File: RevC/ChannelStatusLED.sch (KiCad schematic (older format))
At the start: 6 parts, among them Q1 MBT3946DW1T1, Q2 MBT3946DW1T1, U1 RAx4_4 1K, U2 RAx4_4 1K

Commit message: updates
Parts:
- Q1, Q2: RsComponentsNo (none) -> 791-6078
- R2, R3: LcscNo (none) -> C115295
- U1: LcscNo (none) -> C396839; Type (none) -> N/A
- U1, U2: LcscNo (none) -> C396839
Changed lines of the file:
@@
 $Descr A4 11693 8268
 encoding utf-8
-Sheet 10 29
+Sheet 2 29
 Title ""
 Date ""
@@
 AR Path="/5DDA78A9/5DFDF4A8" Ref="Q15"  Part="2"
 AR Path="/5DDBFE07/5DFDF4A8" Ref="Q17"  Part="2"
-F 0 "Q17" H 4575 1950 50  0000 C CNN
+F 0 "Q1" H 4575 1950 50  0000 C CNN
 F 1 "MBT3946DW1T1" H 4800 1850 50  0000 C CNN
 F 2 "Package_TO_SOT_SMD:SOT-363_SC-70-6" H 4475 2000 50  0001 C CNN
 F 3 "http://www.onsemi.com/pub_link/Collateral/MBT3946DW1T1-D.PDF" H 4275 1900 50  0001 C CNN
+F 4 " 791-6078" H 4275 1900 50  0001 C CNN "RsComponentsNo"
 	2    4275 1900
 	1    0    0    1
@@
 AR Path="/5DDA78A9/5DFDE96B" Ref="Q15"  Part="1"
 AR Path="/5DDBFE07/5DFDE96B" Ref="Q17"  Part="1"
-F 0 "Q17" H 5816 3420 50  0000 L CNN
+F 0 "Q1" H 5816 3420 50  0000 L CNN
 F 1 "MBT3946DW1T1" H 5816 3331 50  0000 L CNN
 F 2 "Package_TO_SOT_SMD:SOT-363_SC-70-6" H 5825 3475 50  0001 C CNN
 F 3 "http://www.onsemi.com/pub_link/Collateral/MBT3946DW1T1-D.PDF" H 5625 3375 50  0001 C CNN
+F 4 " 791-6078" H 5625 3375 50  0001 C CNN "RsComponentsNo"
 	1    5625 3375
 	1    0    0    -1
@@
 AR Path="/5DDA78A9/5DEB0CC3" Ref="#PWR097"  Part="1"
 AR Path="/5DDBFE07/5DEB0CC3" Ref="#PWR099"  Part="1"
-F 0 "#PWR099" H 5725 3675 50  0001 C CNN
+F 0 "#PWR013" H 5725 3675 50  0001 C CNN
 F 1 "GNDS" H 5730 3752 50  0000 C CNN
 F 2 "" H 5725 3925 50  0001 C CNN
@@
 AR Path="/5DDA78A9/5E699B7E" Ref="#PWR035"  Part="1"
 AR Path="/5DDBFE07/5E699B7E" Ref="#PWR037"  Part="1"
-F 0 "#PWR037" H 4375 2400 50  0001 C CNN
+F 0 "#PWR07" H 4375 2400 50  0001 C CNN
 F 1 "GNDS" H 4380 2477 50  0000 C CNN
 F 2 "" H 4375 2650 50  0001 C CNN
@@
 AR Path="/5DDA78A9/5E815CA3" Ref="Q16"  Part="1"
 AR Path="/5DDBFE07/5E815CA3" Ref="Q18"  Part="1"
-F 0 "Q18" H 3740 6196 50  0000 L CNN
+F 0 "Q2" H 3740 6196 50  0000 L CNN
 F 1 "MBT3946DW1T1" H 3740 6105 50  0000 L CNN
 F 2 "Package_TO_SOT_SMD:SOT-363_SC-70-6" H 3750 6250 50  0001 C CNN
 F 3 "http://www.onsemi.com/pub_link/Collateral/MBT3946DW1T1-D.PDF" H 3550 6150 50  0001 C CNN
+F 4 " 791-6078" H 3550 6150 50  0001 C CNN "RsComponentsNo"
 	1    3550 6150
 	1    0    0    -1
@@
 AR Path="/5DDA78A9/5E81663D" Ref="Q16"  Part="2"
 AR Path="/5DDBFE07/5E81663D" Ref="Q18"  Part="2"
-F 0 "Q18" V 7800 5100 50  0000 C CNN
+F 0 "Q2" V 7800 5100 50  0000 C CNN
 F 1 "MBT3946DW1T1" V 7700 5325 50  0000 C CNN
 F 2 "Package_TO_SOT_SMD:SOT-363_SC-70-6" H 8100 4925 50  0001 C CNN
 F 3 "http://www.onsemi.com/pub_link/Collateral/MBT3946DW1T1-D.PDF" H 7900 4825 50  0001 C CNN
+F 4 " 791-6078" V 7900 4825 50  0001 C CNN "RsComponentsNo"
 	2    7900 4825
 	0    1    -1   0
@@
 AR Path="/5DDA78A9/5E819F8C" Ref="#PWR034"  Part="1"
 AR Path="/5DDBFE07/5E819F8C" Ref="#PWR036"  Part="1"
-F 0 "#PWR036" H 3650 7150 50  0001 C CNN
+F 0 "#PWR02" H 3650 7150 50  0001 C CNN
 F 1 "GNDS" H 3655 7227 50  0000 C CNN
 F 2 "" H 3650 7400 50  0001 C CNN
@@
 AR Path="/5DDA78A9/5E833FE4" Ref="R22"  Part="1"
 AR Path="/5DDBFE07/5E833FE4" Ref="R24"  Part="1"
-F 0 "R24" H 9600 4075 50  0000 C CNN
+F 0 "R3" H 9600 4075 50  0000 C CNN
 F 1 "10K" H 9600 4175 50  0000 C CNN
 F 2 "Resistor_SMD:R_0805_2012Metric_Pad1.15x1.40mm_HandSolder" V 9705 4125 50  0001 C CNN
 F 3 "~" H 9775 4125 50  0001 C CNN
+F 4 "C115295" H 9775 4125 50  0001 C CNN "LcscNo"
 	1    9775 4125
 	-1   0    0    1
@@
 AR Path="/5DDA78A9/5E846344" Ref="R21"  Part="1"
 AR Path="/5DDBFE07/5E846344" Ref="R23"  Part="1"
-F 0 "R23" V 2146 6450 50  0000 C CNN
+F 0 "R2" V 2146 6450 50  0000 C CNN
 F 1 "10K" V 2235 6450 50  0000 C CNN
 F 2 "Resistor_SMD:R_0805_2012Metric_Pad1.15x1.40mm_HandSolder" V 2280 6450 50  0001 C CNN
 F 3 "~" H 2350 6450 50  0001 C CNN
+F 4 "C115295" V 2350 6450 50  0001 C CNN "LcscNo"
 	1    2350 6450
 	-1   0    0    1
@@
 AR Path="/5DDA78A9/5E9652F8" Ref="U15"  Part="1"
 AR Path="/5DDBFE07/5E9652F8" Ref="U17"  Part="1"
-F 0 "U17" H 3600 2125 50  0000 C CNN
+F 0 "U1" H 3600 2125 50  0000 C CNN
 F 1 "RAx4_4 1K" H 3600 2034 50  0000 C CNN
 F 2 "Resistor_SMD:R_Array_Convex_4x0603" H 3600 1800 50  0001 C CNN
-F 3 "" H 3600 1900 50  0001 C CNN
+F 3 "https://datasheet.lcsc.com/szlcsc/1912111437_HX-hengjiaxing-HX2301A_C296298.pdf" H 3600 1900 50  0001 C CNN
+F 4 "N/A" H 3600 1900 50  0001 C CNN "Type"
+F 5 "C396839" H 3600 1900 50  0001 C CNN "LcscNo"
 	1    3600 1900
 	1    0    0    -1
@@
 AR Path="/5DDA78A9/5E9687B5" Ref="U15"  Part="2"
 AR Path="/5DDBFE07/5E9687B5" Ref="U17"  Part="2"
-F 0 "U17" H 7175 2218 50  0000 C CNN
+F 0 "U1" H 7175 2218 50  0000 C CNN
 F 1 "RAx4_4 1K" H 7175 2309 50  0000 C CNN
 F 2 "Resistor_SMD:R_Array_Convex_4x0603" H 7175 2325 50  0001 C CNN
-F 3 "" H 7175 2425 50  0001 C CNN
+F 3 "https://datasheet.lcsc.com/szlcsc/1912111437_HX-hengjiaxing-HX2301A_C296298.pdf" H 7175 2425 50  0001 C CNN
+F 4 "C396839" H 7175 2425 50  0001 C CNN "LcscNo"
 	2    7175 2425
 	-1   0    0    1
@@
 AR Path="/5DDA78A9/5E96B96B" Ref="U15"  Part="3"
 AR Path="/5DDBFE07/5E96B96B" Ref="U17"  Part="3"
-F 0 "U17" V 4421 2330 50  0000 R CNN
+F 0 "U1" V 4421 2330 50  0000 R CNN
 F 1 "RAx4_4 1K" V 4330 2330 50  0000 R CNN
 F 2 "Resistor_SMD:R_Array_Convex_4x0603" H 4375 2300 50  0001 C CNN
-F 3 "" H 4375 2400 50  0001 C CNN
+F 3 "https://datasheet.lcsc.com/szlcsc/1912111437_HX-hengjiaxing-HX2301A_C296298.pdf" H 4375 2400 50  0001 C CNN
+F 4 "C396839" V 4375 2400 50  0001 C CNN "LcscNo"
 	3    4375 2400
 	0    -1   -1   0
@@
 AR Path="/5DDA78A9/5E96FE7B" Ref="U15"  Part="4"
 AR Path="/5DDBFE07/5E96FE7B" Ref="U17"  Part="4"
-F 0 "U17" H 3625 3600 50  0000 C CNN
+F 0 "U1" H 3625 3600 50  0000 C CNN
 F 1 "RAx4_4 1K" H 3625 3509 50  0000 C CNN
 F 2 "Resistor_SMD:R_Array_Convex_4x0603" H 3625 3275 50  0001 C CNN
-F 3 "" H 3625 3375 50  0001 C CNN
+F 3 "https://datasheet.lcsc.com/szlcsc/1912111437_HX-hengjiaxing-HX2301A_C296298.pdf" H 3625 3375 50  0001 C CNN
+F 4 "C396839" H 3625 3375 50  0001 C CNN "LcscNo"
 	4    3625 3375
 	1    0    0    -1
@@
 AR Path="/5DDA78A9/5E9776FE" Ref="U16"  Part="2"
 AR Path="/5DDBFE07/5E9776FE" Ref="U18"  Part="2"
-F 0 "U18" V 6854 4463 50  0000 L CNN
+F 0 "U2" V 6854 4463 50  0000 L CNN
 F 1 "RAx4_4 1K" V 6945 4463 50  0000 L CNN
 F 2 "Resistor_SMD:R_Array_Convex_4x0603" H 6900 4275 50  0001 C CNN
-F 3 "" H 6900 4375 50  0001 C CNN
+F 3 "https://datasheet.lcsc.com/szlcsc/1912111437_HX-hengjiaxing-HX2301A_C296298.pdf" H 6900 4375 50  0001 C CNN
+F 4 "C396839" V 6900 4375 50  0001 C CNN "LcscNo"
 	2    6900 4375
 	0    1    1    0
@@
 AR Path="/5DDA78A9/5E99998D" Ref="U16"  Part="3"
 AR Path="/5DDBFE07/5E99998D" Ref="U18"  Part="3"
-F 0 "U18" H 2950 6375 50  0000 C CNN
+F 0 "U2" H 2950 6375 50  0000 C CNN
 F 1 "RAx4_4 1K" H 2950 6284 50  0000 C CNN
 F 2 "Resistor_SMD:R_Array_Convex_4x0603" H 2950 6050 50  0001 C CNN
-F 3 "" H 2950 6150 50  0001 C CNN
+F 3 "https://datasheet.lcsc.com/szlcsc/1912111437_HX-hengjiaxing-HX2301A_C296298.pdf" H 2950 6150 50  0001 C CNN
+F 4 "C396839" H 2950 6150 50  0001 C CNN "LcscNo"
 	3    2950 6150
 	1    0    0    -1
@@
 AR Path="/5DDA78A9/5EAAD0E5" Ref="U16"  Part="4"
 AR Path="/5DDBFE07/5EAAD0E5" Ref="U18"  Part="4"
-F 0 "U18" V 3696 6880 50  0000 R CNN
+F 0 "U2" V 3696 6880 50  0000 R CNN
 F 1 "RAx4_4 1K" V 3605 6880 50  0000 R CNN
 F 2 "Resistor_SMD:R_Array_Convex_4x0603" H 3650 6850 50  0001 C CNN
-F 3 "" H 3650 6950 50  0001 C CNN
+F 3 "https://datasheet.lcsc.com/szlcsc/1912111437_HX-hengjiaxing-HX2301A_C296298.pdf" H 3650 6950 50  0001 C CNN
+F 4 "C396839" V 3650 6950 50  0001 C CNN "LcscNo"
 	4    3650 6950
 	0    -1   -1   0
@@
 AR Path="/5DDA78A9/5E033493" Ref="#PWR0149"  Part="1"
 AR Path="/5DDBFE07/5E033493" Ref="#PWR0150"  Part="1"
-F 0 "#PWR0150" H 2350 6900 50  0001 C CNN
+F 0 "#PWR0115" H 2350 6900 50  0001 C CNN
 F 1 "GNDS" H 2355 6977 50  0000 C CNN
 F 2 "" H 2350 7150 50  0001 C CNN

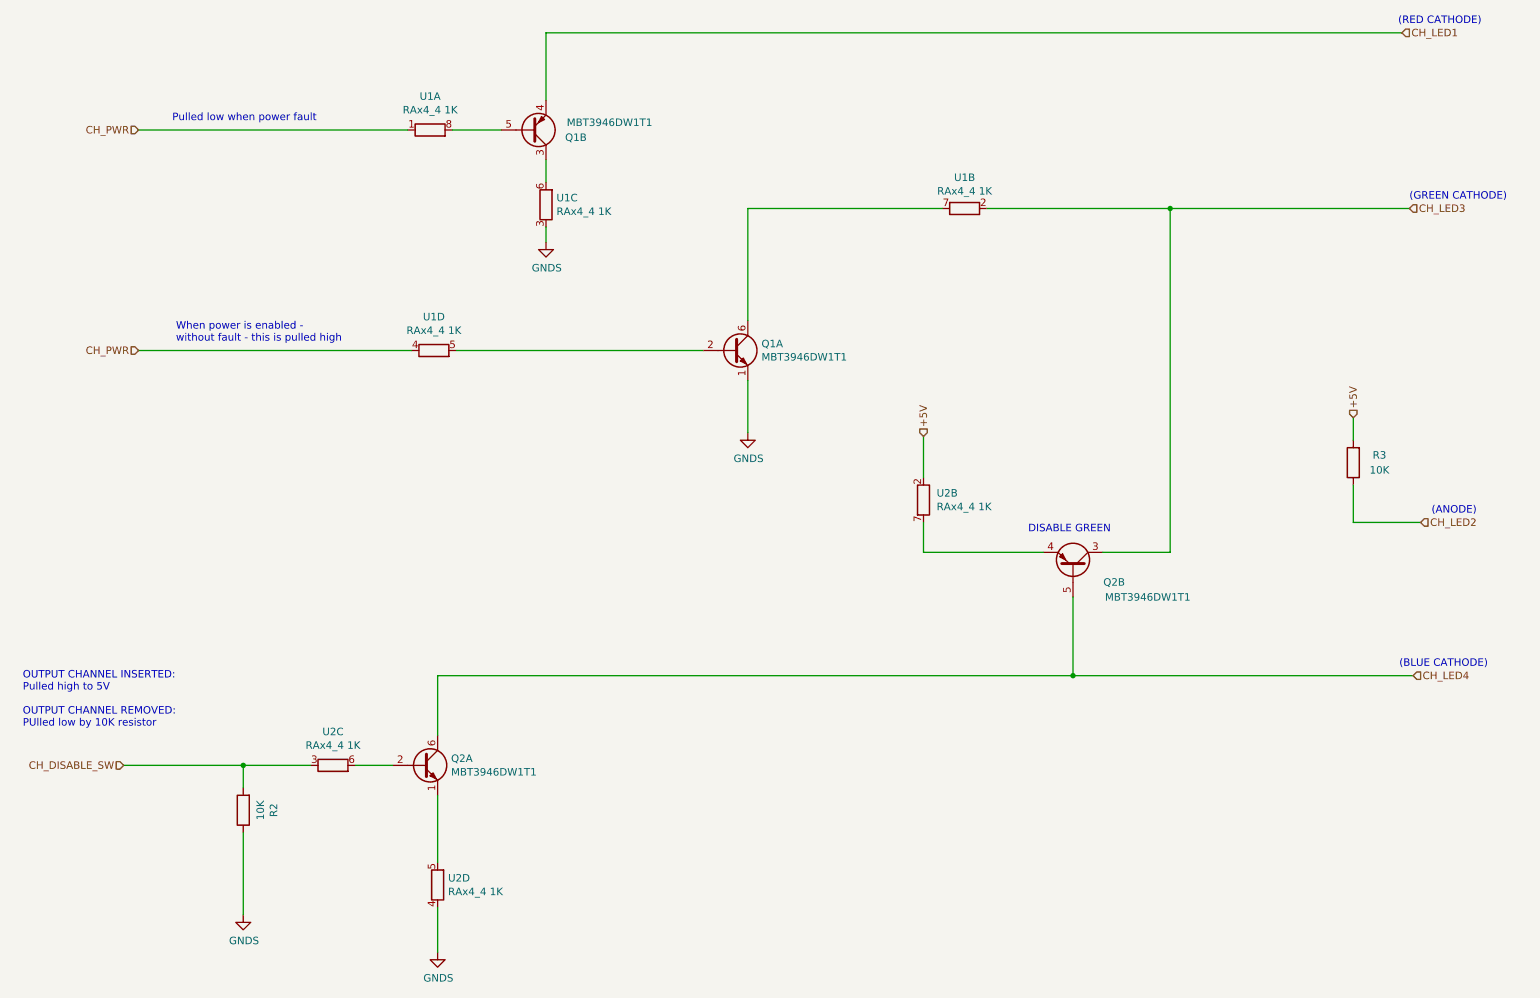
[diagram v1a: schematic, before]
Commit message: Replaced 6N135 SMDIP8 with H11L1 SMDIP6
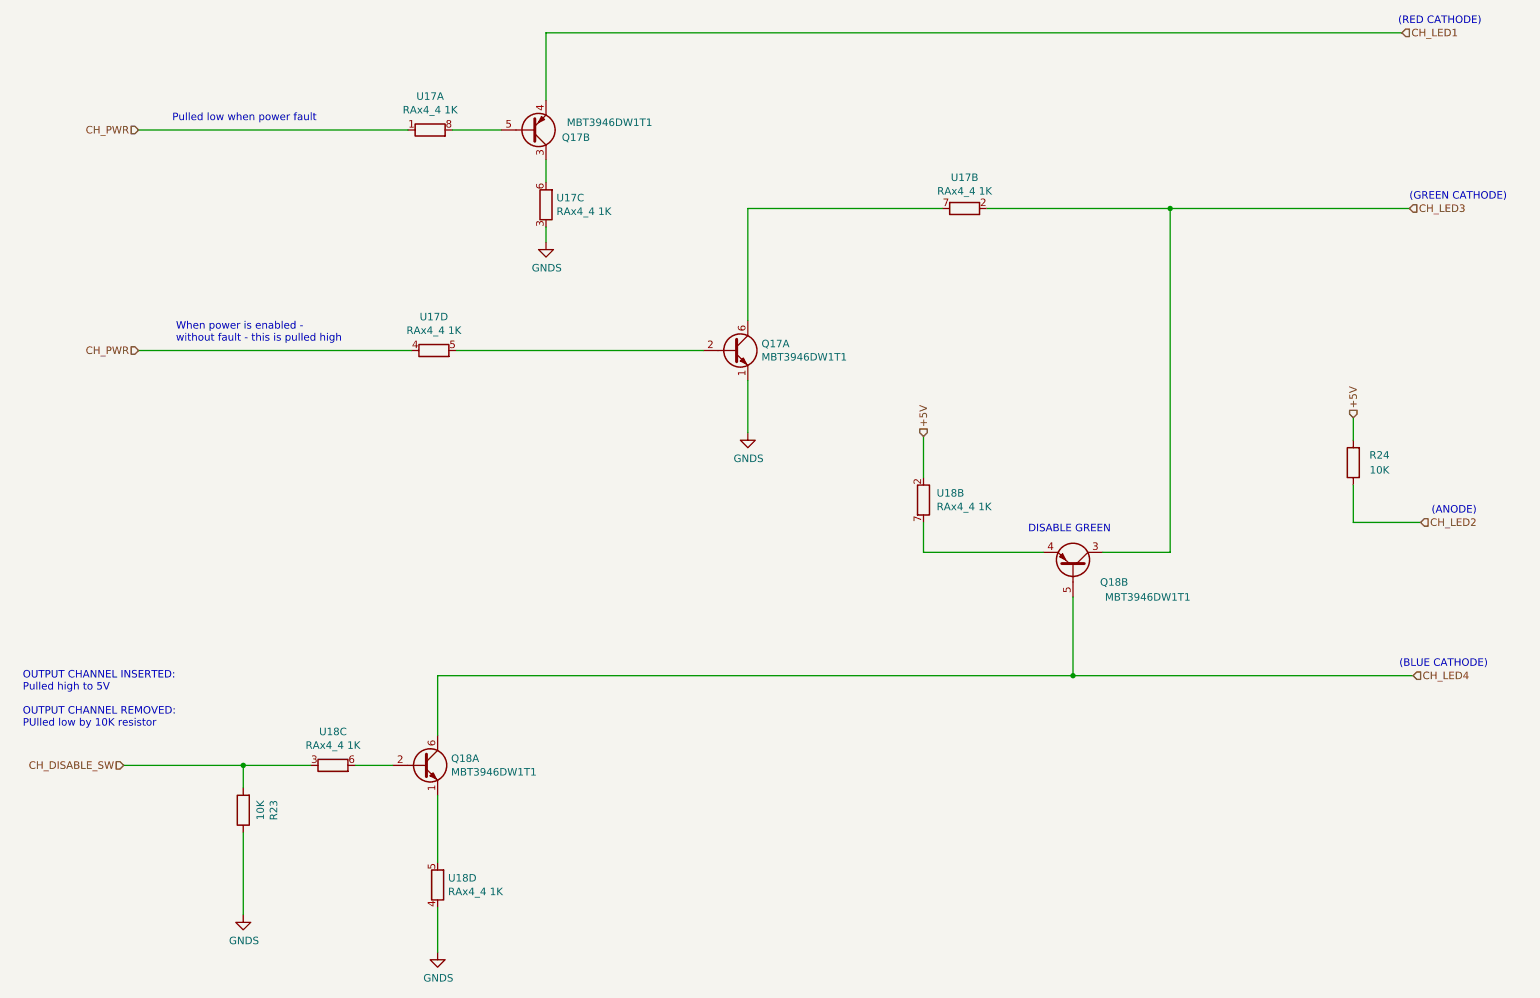
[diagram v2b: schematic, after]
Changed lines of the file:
@@
 AR Path="/5DDA78A9/5DFDF4A8" Ref="Q15"  Part="2"
 AR Path="/5DDBFE07/5DFDF4A8" Ref="Q17"  Part="2"
-F 0 "Q1" H 4575 1950 50  0000 C CNN
+F 0 "Q17" H 4575 1950 50  0000 C CNN
 F 1 "MBT3946DW1T1" H 4800 1850 50  0000 C CNN
 F 2 "Package_TO_SOT_SMD:SOT-363_SC-70-6" H 4475 2000 50  0001 C CNN
@@
 AR Path="/5DDA78A9/5DFDE96B" Ref="Q15"  Part="1"
 AR Path="/5DDBFE07/5DFDE96B" Ref="Q17"  Part="1"
-F 0 "Q1" H 5816 3420 50  0000 L CNN
+F 0 "Q17" H 5816 3420 50  0000 L CNN
 F 1 "MBT3946DW1T1" H 5816 3331 50  0000 L CNN
 F 2 "Package_TO_SOT_SMD:SOT-363_SC-70-6" H 5825 3475 50  0001 C CNN
@@
 AR Path="/5DDA78A9/5DEB0CC3" Ref="#PWR097"  Part="1"
 AR Path="/5DDBFE07/5DEB0CC3" Ref="#PWR099"  Part="1"
-F 0 "#PWR013" H 5725 3675 50  0001 C CNN
+F 0 "#PWR099" H 5725 3675 50  0001 C CNN
 F 1 "GNDS" H 5730 3752 50  0000 C CNN
 F 2 "" H 5725 3925 50  0001 C CNN
@@
 AR Path="/5DDA78A9/5E699B7E" Ref="#PWR035"  Part="1"
 AR Path="/5DDBFE07/5E699B7E" Ref="#PWR037"  Part="1"
-F 0 "#PWR07" H 4375 2400 50  0001 C CNN
+F 0 "#PWR037" H 4375 2400 50  0001 C CNN
 F 1 "GNDS" H 4380 2477 50  0000 C CNN
 F 2 "" H 4375 2650 50  0001 C CNN
@@
 AR Path="/5DDA78A9/5E815CA3" Ref="Q16"  Part="1"
 AR Path="/5DDBFE07/5E815CA3" Ref="Q18"  Part="1"
-F 0 "Q2" H 3740 6196 50  0000 L CNN
+F 0 "Q18" H 3740 6196 50  0000 L CNN
 F 1 "MBT3946DW1T1" H 3740 6105 50  0000 L CNN
 F 2 "Package_TO_SOT_SMD:SOT-363_SC-70-6" H 3750 6250 50  0001 C CNN
@@
 AR Path="/5DDA78A9/5E81663D" Ref="Q16"  Part="2"
 AR Path="/5DDBFE07/5E81663D" Ref="Q18"  Part="2"
-F 0 "Q2" V 7800 5100 50  0000 C CNN
+F 0 "Q18" V 7800 5100 50  0000 C CNN
 F 1 "MBT3946DW1T1" V 7700 5325 50  0000 C CNN
 F 2 "Package_TO_SOT_SMD:SOT-363_SC-70-6" H 8100 4925 50  0001 C CNN
@@
 AR Path="/5DDA78A9/5E819F8C" Ref="#PWR034"  Part="1"
 AR Path="/5DDBFE07/5E819F8C" Ref="#PWR036"  Part="1"
-F 0 "#PWR02" H 3650 7150 50  0001 C CNN
+F 0 "#PWR036" H 3650 7150 50  0001 C CNN
 F 1 "GNDS" H 3655 7227 50  0000 C CNN
 F 2 "" H 3650 7400 50  0001 C CNN
@@
 AR Path="/5DDA78A9/5E833FE4" Ref="R22"  Part="1"
 AR Path="/5DDBFE07/5E833FE4" Ref="R24"  Part="1"
-F 0 "R3" H 9600 4075 50  0000 C CNN
+F 0 "R24" H 9600 4075 50  0000 C CNN
 F 1 "10K" H 9600 4175 50  0000 C CNN
 F 2 "Resistor_SMD:R_0805_2012Metric_Pad1.15x1.40mm_HandSolder" V 9705 4125 50  0001 C CNN
@@
 AR Path="/5DDA78A9/5E846344" Ref="R21"  Part="1"
 AR Path="/5DDBFE07/5E846344" Ref="R23"  Part="1"
-F 0 "R2" V 2146 6450 50  0000 C CNN
+F 0 "R23" V 2146 6450 50  0000 C CNN
 F 1 "10K" V 2235 6450 50  0000 C CNN
 F 2 "Resistor_SMD:R_0805_2012Metric_Pad1.15x1.40mm_HandSolder" V 2280 6450 50  0001 C CNN
@@
 AR Path="/5DDA78A9/5E9652F8" Ref="U15"  Part="1"
 AR Path="/5DDBFE07/5E9652F8" Ref="U17"  Part="1"
-F 0 "U1" H 3600 2125 50  0000 C CNN
+F 0 "U17" H 3600 2125 50  0000 C CNN
 F 1 "RAx4_4 1K" H 3600 2034 50  0000 C CNN
 F 2 "Resistor_SMD:R_Array_Convex_4x0603" H 3600 1800 50  0001 C CNN
@@
 AR Path="/5DDA78A9/5E9687B5" Ref="U15"  Part="2"
 AR Path="/5DDBFE07/5E9687B5" Ref="U17"  Part="2"
-F 0 "U1" H 7175 2218 50  0000 C CNN
+F 0 "U17" H 7175 2218 50  0000 C CNN
 F 1 "RAx4_4 1K" H 7175 2309 50  0000 C CNN
 F 2 "Resistor_SMD:R_Array_Convex_4x0603" H 7175 2325 50  0001 C CNN
@@
 AR Path="/5DDA78A9/5E96B96B" Ref="U15"  Part="3"
 AR Path="/5DDBFE07/5E96B96B" Ref="U17"  Part="3"
-F 0 "U1" V 4421 2330 50  0000 R CNN
+F 0 "U17" V 4421 2330 50  0000 R CNN
 F 1 "RAx4_4 1K" V 4330 2330 50  0000 R CNN
 F 2 "Resistor_SMD:R_Array_Convex_4x0603" H 4375 2300 50  0001 C CNN
@@
 AR Path="/5DDA78A9/5E96FE7B" Ref="U15"  Part="4"
 AR Path="/5DDBFE07/5E96FE7B" Ref="U17"  Part="4"
-F 0 "U1" H 3625 3600 50  0000 C CNN
+F 0 "U17" H 3625 3600 50  0000 C CNN
 F 1 "RAx4_4 1K" H 3625 3509 50  0000 C CNN
 F 2 "Resistor_SMD:R_Array_Convex_4x0603" H 3625 3275 50  0001 C CNN
@@
 AR Path="/5DDA78A9/5E9776FE" Ref="U16"  Part="2"
 AR Path="/5DDBFE07/5E9776FE" Ref="U18"  Part="2"
-F 0 "U2" V 6854 4463 50  0000 L CNN
+F 0 "U18" V 6854 4463 50  0000 L CNN
 F 1 "RAx4_4 1K" V 6945 4463 50  0000 L CNN
 F 2 "Resistor_SMD:R_Array_Convex_4x0603" H 6900 4275 50  0001 C CNN
@@
 AR Path="/5DDA78A9/5E99998D" Ref="U16"  Part="3"
 AR Path="/5DDBFE07/5E99998D" Ref="U18"  Part="3"
-F 0 "U2" H 2950 6375 50  0000 C CNN
+F 0 "U18" H 2950 6375 50  0000 C CNN
 F 1 "RAx4_4 1K" H 2950 6284 50  0000 C CNN
 F 2 "Resistor_SMD:R_Array_Convex_4x0603" H 2950 6050 50  0001 C CNN
@@
 AR Path="/5DDA78A9/5EAAD0E5" Ref="U16"  Part="4"
 AR Path="/5DDBFE07/5EAAD0E5" Ref="U18"  Part="4"
-F 0 "U2" V 3696 6880 50  0000 R CNN
+F 0 "U18" V 3696 6880 50  0000 R CNN
 F 1 "RAx4_4 1K" V 3605 6880 50  0000 R CNN
 F 2 "Resistor_SMD:R_Array_Convex_4x0603" H 3650 6850 50  0001 C CNN
@@
 AR Path="/5DDA78A9/5E033493" Ref="#PWR0149"  Part="1"
 AR Path="/5DDBFE07/5E033493" Ref="#PWR0150"  Part="1"
-F 0 "#PWR0115" H 2350 6900 50  0001 C CNN
+F 0 "#PWR0150" H 2350 6900 50  0001 C CNN
 F 1 "GNDS" H 2355 6977 50  0000 C CNN
 F 2 "" H 2350 7150 50  0001 C CNN
